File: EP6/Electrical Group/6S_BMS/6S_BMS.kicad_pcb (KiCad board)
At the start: 4 copper layers, 197 parts, among them IC1 DZDH0401DW-7, IC2 DZDH0401DW-7, J1 BATcellMain, J10 CAN1, J11 frontBox, J12 switch, J13 RESET, J14 battery cells, J2 BAT charge, J3 GLVMS, J4 24Vout, J5 USB_C_stm32, J6 UART2, J7 I2C1, J8 7seg, J9 SWD, Q1 SI2301CDS-T1-GE3, Q10 HSBA3119, Q11 2N7002, Q12 2N7002, Q13 AO3401A, Q14 2N7002, Q15 HSBA3119, Q16 HSBA3119, Q17 HSBA3119, Q2 SI2301CDS-T1-GE3, Q3 SI2301CDS-T1-GE3, Q4 SI2301CDS-T1-GE3, Q5 SI2301CDS-T1-GE3, Q6 SI2301CDS-T1-GE3, Q9 2N7002, SW1 RESET, U1 LM66100DCK, U2 BQ7693003, U3 STM32F103C8Tx, U4 78L05G-AB3-R, U5 HT7533, U6 TCAN1042VDRQ1, Y1 8MHz X49SM8MSD2SC

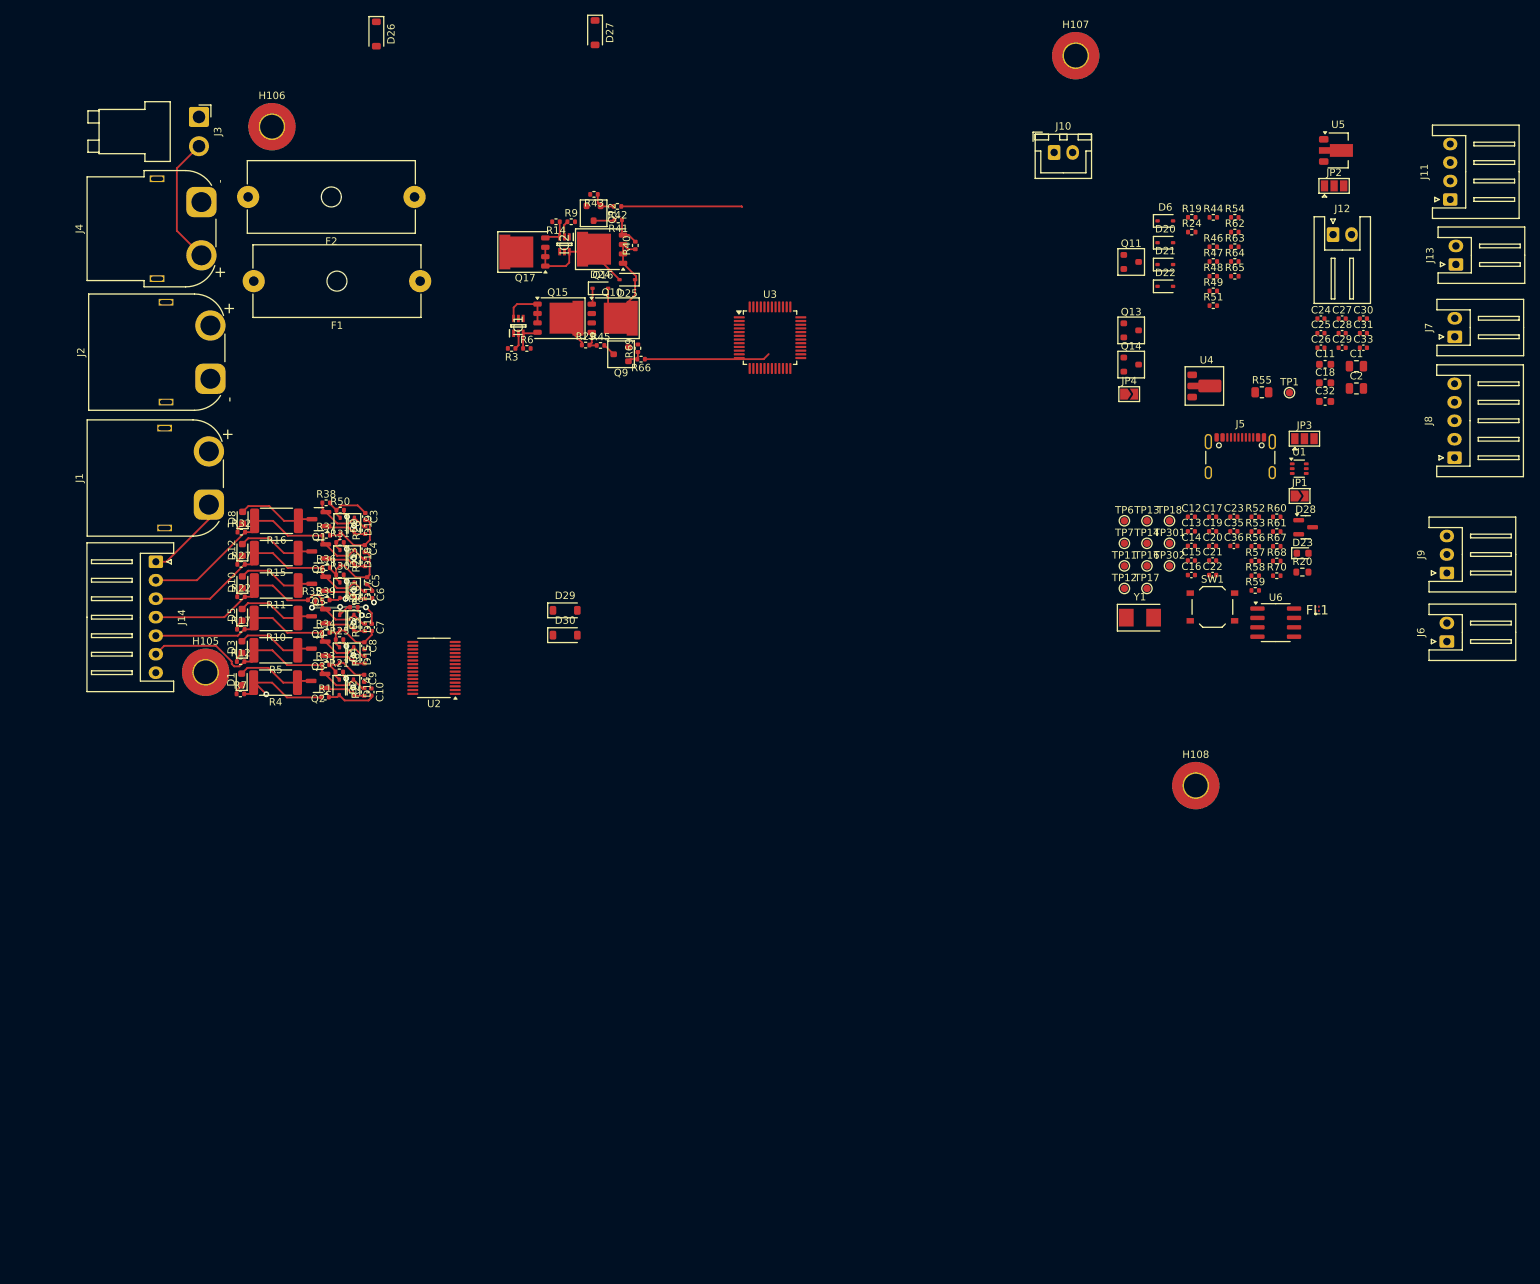
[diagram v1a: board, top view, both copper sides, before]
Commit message: added nickel tabs footprint, assigned footprints
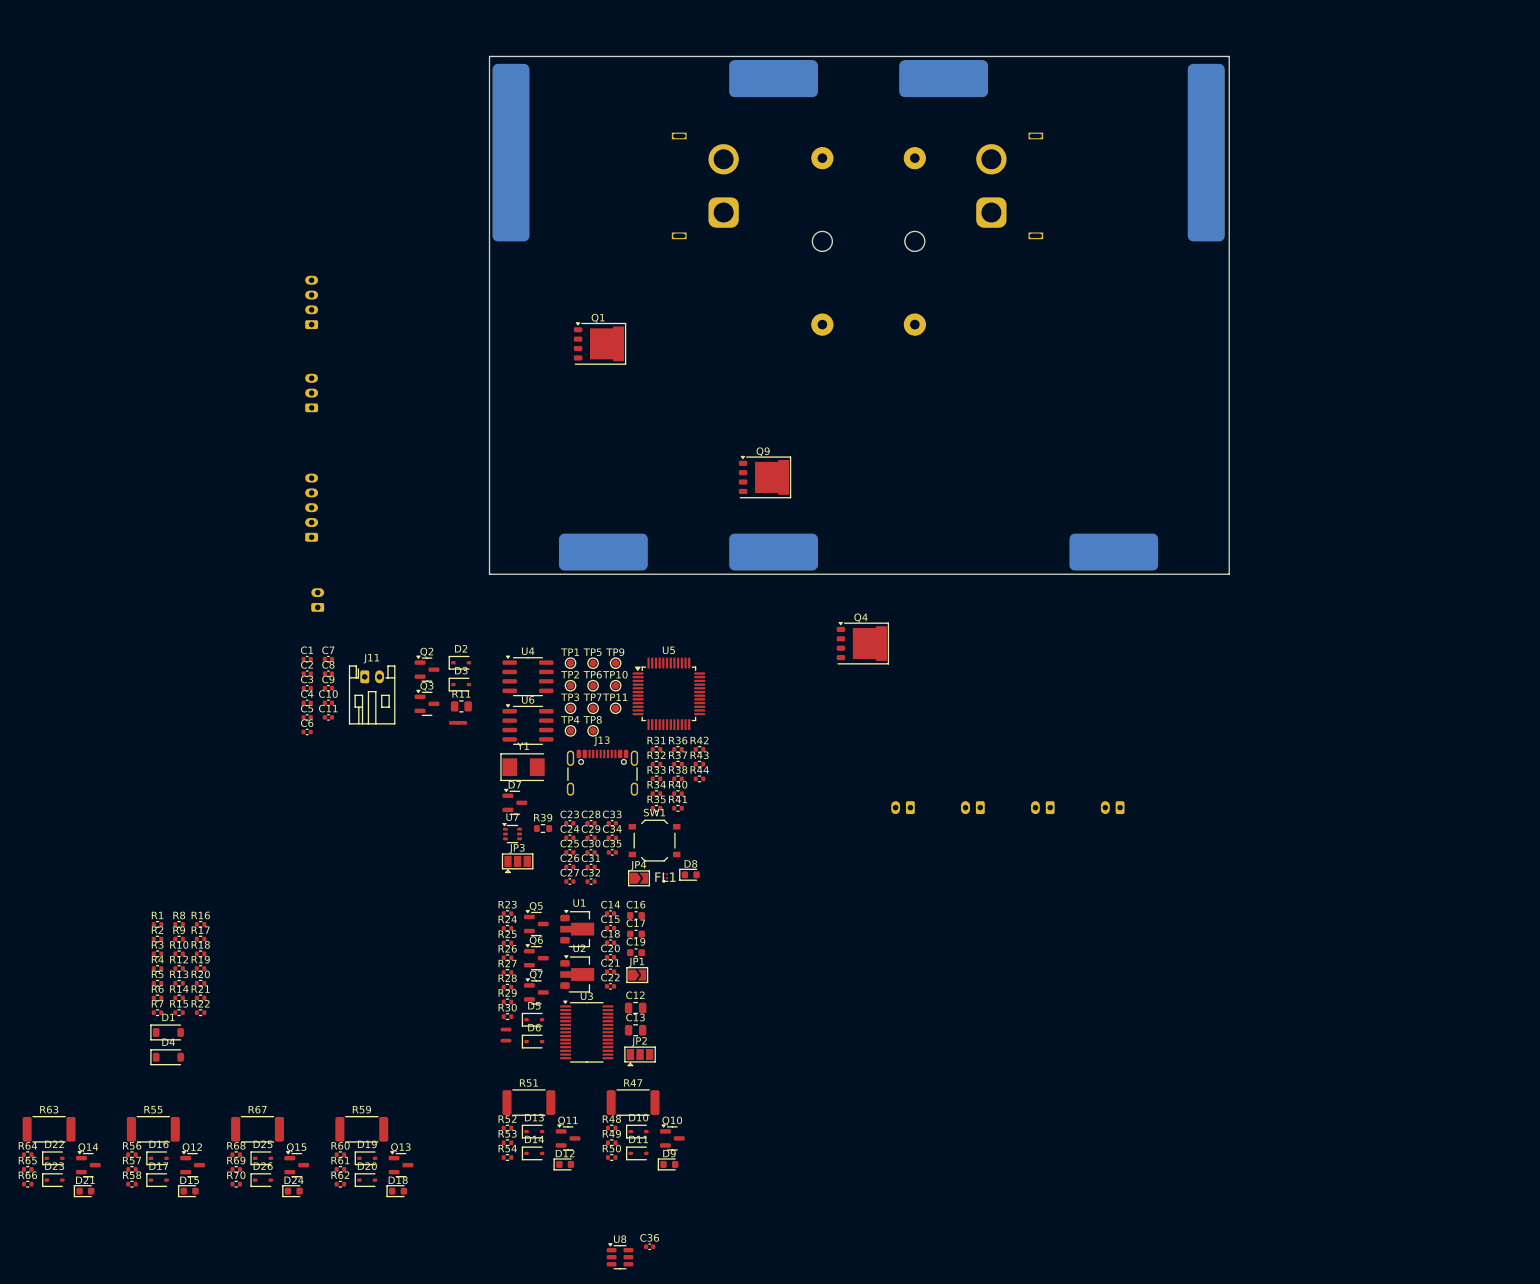
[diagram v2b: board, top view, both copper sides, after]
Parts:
- removed D27, D29, D30: 27V, Diode_SMD:D_SOD-123
- removed D28: NUP2105L, Package_TO_SOT_SMD:SOT-23
- removed H105, H106, H107, H108: MountingHole_Pad, MountingHole:MountingHole_3.2mm_M3_Pad_TopBottom
- removed IC1, IC2: DZDH0401DW-7, SamacSys_Parts_EP6:SOT65P210X110-6N
- removed J14: battery cells, Connector_JST:JST_XH_S7B-XH-A_1x07_P2.50mm_Horizontal
- removed Q16, Q17: HSBA3119, nturt_kicad_lib_EP6:HSBA3119_PRPAK5X6
- removed R45: 100k, Resistor_SMD:R_0402_1005Metric
- removed R46: 10k, Resistor_SMD:R_0402_1005Metric
- removed TP12: SPI2_MISO, TestPoint:TestPoint_Pad_D1.0mm
- removed TP13: SPI2_SCK, TestPoint:TestPoint_Pad_D1.0mm
- removed TP14: CAN1_S, TestPoint:TestPoint_Pad_D1.0mm
- removed TP16: SPI2_CSN, TestPoint:TestPoint_Pad_D1.0mm
- removed TP17: I2C1_SCL, TestPoint:TestPoint_Pad_D1.0mm
- removed TP18: I2C1_SDA, TestPoint:TestPoint_Pad_D1.0mm
- removed TP301: CAN1_RX, TestPoint:TestPoint_Pad_D1.0mm
- removed TP302: CAN1_TX, TestPoint:TestPoint_Pad_D1.0mm
- added C34: 0u1, Capacitor_SMD:C_0402_1005Metric, F.Cu at (116.6, 130.6)
- added NT1: CELL_NEG_TIE, NetTie:NetTie-3_SMD_Pad0.5mm, F.Cu at (95.7, 115.1)
- added NT2: NetTie_2, NetTie:NetTie-2_SMD_Pad0.5mm, F.Cu at (102.2, 156.6)
- added NT3: NetTie_2, NetTie:NetTie-2_SMD_Pad0.5mm, F.Cu at (102.2, 158.1)
- added Q7: AO3401A, Package_TO_SOT_SMD:SOT-23, F.Cu at (106.3, 151.5)
- added TP10: UART1_TX, TestPoint:TestPoint_Pad_D1.0mm, F.Cu at (117.1, 110.1)
- added TP2: CAN1_S, TestPoint:TestPoint_Pad_D1.0mm, F.Cu at (111.0, 110.1)
- added TP3: SPI2_CSN, TestPoint:TestPoint_Pad_D1.0mm, F.Cu at (111.0, 113.1)
- added TP4: SPI2_MISO, TestPoint:TestPoint_Pad_D1.0mm, F.Cu at (111.0, 116.2)
- added TP5: I2C1_SDA, TestPoint:TestPoint_Pad_D1.0mm, F.Cu at (114.0, 107.0)
- added TP8: SPI2_MOSI, TestPoint:TestPoint_Pad_D1.0mm, F.Cu at (114.0, 116.2)
- added TP9: CAN1_RX, TestPoint:TestPoint_Pad_D1.0mm, F.Cu at (117.1, 107.0)
- added U7: LM66100DCK, Package_TO_SOT_SMD:SOT-363_SC-70-6, F.Cu at (103.1, 130.1)
- added U8: LM74700, Package_TO_SOT_SMD:SOT-23-6, F.Cu at (117.6, 187.3)
- C1, C2: value 10u 25V -> 1u; footprint Capacitor_SMD:C_0805_2012Metric -> Capacitor_SMD:C_0402_1005Metric
- C10, C25, C26, C9: value 1u -> 0u1
- C11: value 1u -> 0u1; footprint Capacitor_SMD:C_0603_1608Metric -> Capacitor_SMD:C_0402_1005Metric
- C12, C13: value 30p -> 10u 25V; footprint Capacitor_SMD:C_0402_1005Metric -> Capacitor_SMD:C_0805_2012Metric
- C14: value 10u 6V -> 1u
- C15, C20, C21: value 0u1 -> 1u
- C16: value 10u 6V -> 10u; footprint Capacitor_SMD:C_0402_1005Metric -> Capacitor_SMD:C_0603_1608Metric
- C17: value 10u 6V -> 4u7 16V; footprint Capacitor_SMD:C_0402_1005Metric -> Capacitor_SMD:C_0603_1608Metric
- C18: value 4u7 16V -> 10u; footprint Capacitor_SMD:C_0603_1608Metric -> Capacitor_SMD:C_0402_1005Metric
- C19: value 10u 6V -> 1u; footprint Capacitor_SMD:C_0402_1005Metric -> Capacitor_SMD:C_0603_1608Metric
- C22: value 0u1 -> 470p
- C24: value 470p -> 30p
- C27: value 0u1 -> 30p
- C28, C29, C31: value 0u1 -> 10u 6V
- C30: value 1u -> 10u 6V
- C32: value 10u -> 0u1; footprint Capacitor_SMD:C_0603_1608Metric -> Capacitor_SMD:C_0402_1005Metric
- C33: value 10u -> 0u1
- C36: value 0u1 -> 220nF 25V
- D1: value RED -> 27V; footprint LED_SMD:LED_0603_1608Metric -> Diode_SMD:D_SOD-123
- D10: value RED -> BZT52C6V8S; footprint LED_SMD:LED_0603_1608Metric -> Diode_SMD:D_SOD-323
- D12: value RED -> BAL_1
- D15, D18, D9: value BZT52C6V8S -> BAL_1; footprint Diode_SMD:D_SOD-323 -> LED_SMD:LED_0603_1608Metric
- D2: value BZT52C6V8S -> 1N4148WS
- D20: value 1N4148WS -> BZT52C6V8S
- D21: value 1N4148WS -> BAL_1; footprint Diode_SMD:D_SOD-323 -> LED_SMD:LED_0603_1608Metric
- D22: value BZX584C3V3 -> BZT52C6V8S
- D23: value WHITE -> BZT52C6V8S; footprint LED_SMD:LED_0603_1608Metric -> Diode_SMD:D_SOD-323
- D24: value 27V -> BAL_1; footprint Diode_SMD:D_SOD-323 -> LED_SMD:LED_0603_1608Metric
- D25: value 27V -> BZT52C6V8S
- D26: value 27V -> BZT52C6V8S; footprint Diode_SMD:D_SOD-123 -> Diode_SMD:D_SOD-323
- D3: value RED -> BZX584C3V3; footprint LED_SMD:LED_0603_1608Metric -> Diode_SMD:D_SOD-323
- D4: value BZT52C6V8S -> 27V; footprint Diode_SMD:D_SOD-323 -> Diode_SMD:D_SOD-123
- D5: value RED -> 1N4148WS; footprint LED_SMD:LED_0603_1608Metric -> Diode_SMD:D_SOD-323
- D7: value BZT52C6V8S -> NUP2105L; footprint Diode_SMD:D_SOD-323 -> Package_TO_SOT_SMD:SOT-23
- D8: value RED -> WHITE
- F1: value 10A charge fuse -> 10A battery fuse; moved to B.Cu
- F2: value 10A discharge fuse -> 10A ext fuse; moved to B.Cu
- J1: value BATcellMain -> battery cells; footprint Connector_AMASS:AMASS_XT60PW-M_1x02_P7.20mm_Horizontal -> nturt_kicad_lib_EP6:6S_batteries_100mm_across; moved to B.Cu
- J10: value CAN1 -> I2C1; footprint Connector_JST:JST_XH_B2B-XH-A_1x02_P2.50mm_Vertical -> Connector_JST:JST_PH_S2B-PH-K_1x02_P2.00mm_Horizontal; moved to B.Cu
- J11: value frontBox -> CAN1; footprint Connector_JST:JST_XH_S4B-XH-A_1x04_P2.50mm_Horizontal -> Connector_JST:JST_PH_S2B-PH-K_1x02_P2.00mm_Horizontal
- J12: value switch -> frontBox; footprint Connector_JST:JST_XH_S2B-XH-A_1x02_P2.50mm_Horizontal -> Connector_JST:JST_PH_S4B-PH-K_1x04_P2.00mm_Horizontal; moved to B.Cu
- J13: value RESET -> USB_C_stm32; footprint Connector_JST:JST_XH_S2B-XH-A_1x02_P2.50mm_Horizontal -> Connector_USB:USB_C_Receptacle_GCT_USB4105-xx-A_16P_TopMnt_Horizontal
- J2: value BAT charge -> GLVMS; footprint Connector_AMASS:AMASS_XT60PW-M_1x02_P7.20mm_Horizontal -> Connector_JST:JST_PH_S2B-PH-K_1x02_P2.00mm_Horizontal; moved to B.Cu
- J3: value GLVMS -> BOOT_BTN; footprint Connector_JST:JST_VH_B2PS-VH_1x02_P3.96mm_Horizontal -> Connector_JST:JST_PH_S2B-PH-K_1x02_P2.00mm_Horizontal; moved to B.Cu
- J4: moved to B.Cu
- J5: value USB_C_stm32 -> CHARGE; footprint Connector_USB:USB_C_Receptacle_GCT_USB4105-xx-A_16P_TopMnt_Horizontal -> Connector_AMASS:AMASS_XT60PW-M_1x02_P7.20mm_Horizontal; moved to B.Cu
- J6: footprint Connector_JST:JST_XH_S2B-XH-A_1x02_P2.50mm_Horizontal -> Connector_JST:JST_PH_S2B-PH-K_1x02_P2.00mm_Horizontal; moved to B.Cu
- J7: value I2C1 -> SWD; footprint Connector_JST:JST_XH_S2B-XH-A_1x02_P2.50mm_Horizontal -> Connector_JST:JST_PH_S3B-PH-K_1x03_P2.00mm_Horizontal; moved to B.Cu
- J8: footprint Connector_JST:JST_XH_S5B-XH-A_1x05_P2.50mm_Horizontal -> Connector_JST:JST_PH_S5B-PH-K_1x05_P2.00mm_Horizontal; moved to B.Cu
- J9: value SWD -> RESET; footprint Connector_JST:JST_XH_S3B-XH-A_1x03_P2.50mm_Horizontal -> Connector_JST:JST_PH_S2B-PH-K_1x02_P2.00mm_Horizontal; moved to B.Cu
- JP1: value Vbus -> REGSRC bypass
- JP2: value 3V3 source -> 3V3 select
- JP4: value REGSRC bypass -> Vbus
- Q1, Q4: value SI2301CDS-T1-GE3 -> HSBA3119; footprint Package_TO_SOT_SMD:SOT-23 -> nturt_kicad_lib_EP6:HSBA3119_PRPAK5X6
- Q10, Q15: value HSBA3119 -> SI2301CDS-T1-GE3; footprint nturt_kicad_lib_EP6:HSBA3119_PRPAK5X6 -> Package_TO_SOT_SMD:SOT-23
- Q11, Q12, Q14: value 2N7002 -> SI2301CDS-T1-GE3; footprint PCM_Package_TO_SOT_SMD_AKL:SOT-23 -> Package_TO_SOT_SMD:SOT-23
- Q13: value AO3401A -> SI2301CDS-T1-GE3; footprint PCM_Package_TO_SOT_SMD_AKL:SOT-23 -> Package_TO_SOT_SMD:SOT-23
- Q2, Q3, Q5, Q6: value SI2301CDS-T1-GE3 -> 2N7002
- Q9: value 2N7002 -> HSBA3119; footprint PCM_Package_TO_SOT_SMD_AKL:SOT-23 -> nturt_kicad_lib_EP6:HSBA3119_PRPAK5X6
- R10: value 10R 2W 2512 -> 100k; footprint Resistor_SMD:R_2512_6332Metric -> Resistor_SMD:R_0402_1005Metric
- R11: value 10R 2W 2512 -> 10R 1%; footprint Resistor_SMD:R_2512_6332Metric -> Resistor_SMD:R_0805_2012Metric
- R13, R2, R8: value 2M -> 1k
- R14: value Rbias -> 100R
- R15, R16: value 10R 2W 2512 -> 1M; footprint Resistor_SMD:R_2512_6332Metric -> Resistor_SMD:R_0402_1005Metric
- R17: value 1k -> 100k
- R18: value 2M -> 100k
- R19: value 100R -> 100k
- R20: value 1k -> 4k3; footprint Resistor_SMD:R_0603_1608Metric -> Resistor_SMD:R_0402_1005Metric
- R21: value 1k -> 15k
- R22: value 1k -> 47k
- R23: value 2M -> 100R
- R26: value 1k -> 1M
- R27: value 1k -> 470k
- R28: value 2M -> 1M
- R29, R40: value 100k -> 10k
- R3: value Rref -> 1k
- R30: value 1k -> 500k
- R31, R32, R36: value 1k -> 10k
- R34, R35: value 1k -> 100R
- R37, R38: value 1k -> 4k7
- R39: footprint Resistor_SMD:R_0402_1005Metric -> Resistor_SMD:R_0603_1608Metric
- R4, R5: value 10R 2W 2512 -> 1k; footprint Resistor_SMD:R_2512_6332Metric -> Resistor_SMD:R_0402_1005Metric
- R41: value 100k -> 10R
- R42: value 1k -> 10R
- R43: value 1M -> 5k1
- R44: value 500k -> 5k1
- R47: value 10k -> 10R 2W 2512; footprint Resistor_SMD:R_0402_1005Metric -> Resistor_SMD:R_2512_6332Metric
- R48, R52, R56, R70: value 10k -> 1k
- R49, R53: value 10k -> 2M
- R51, R67: value 100R -> 10R 2W 2512; footprint Resistor_SMD:R_0402_1005Metric -> Resistor_SMD:R_2512_6332Metric
- R54, R68: value 100R -> 1k
- R55: value 10R 1% -> 10R 2W 2512; footprint Resistor_SMD:R_0805_2012Metric -> Resistor_SMD:R_2512_6332Metric
- R57: value 5k1 -> 2M
- R58: value 5k1 -> 1k
- R59: value 10R -> 10R 2W 2512; footprint Resistor_SMD:R_0402_1005Metric -> Resistor_SMD:R_2512_6332Metric
- R6: value Rbias -> 1k
- R60: value 10R -> 1k
- R61: value 1k -> 2M
- R62: value 1M -> 1k
- R63: value 1M -> 10R 2W 2512; footprint Resistor_SMD:R_0402_1005Metric -> Resistor_SMD:R_2512_6332Metric
- R65, R69: value 1M -> 2M
- R9: value Rref -> 100R
- TP1: value REGOUT -> I2C1_SCL
- TP11: value SPI2_MOSI -> UART1_RX
- TP6: value UART1_TX -> CAN1_TX
- TP7: value UART1_RX -> SPI2_SCK
- U1: value LM66100DCK -> 78L05G-AB3-R; footprint Package_TO_SOT_SMD:SOT-363_SC-70-6 -> Package_TO_SOT_SMD:SOT-89-3
- U2: value BQ7693003 -> HT7533; footprint Package_SO:TSSOP-30_4.4x7.8mm_P0.5mm -> Package_TO_SOT_SMD:SOT-89-3
- U3: value STM32F103C8Tx -> BQ7693003; footprint Package_QFP:LQFP-48_7x7mm_P0.5mm -> Package_SO:TSSOP-30_4.4x7.8mm_P0.5mm
- U4: value 78L05G-AB3-R -> TCAN1042VDRQ1; footprint PCM_Package_TO_SOT_SMD_AKL:SOT-89-3 -> Package_SO:SOIC-8_3.9x4.9mm_P1.27mm
- U5: value HT7533 -> STM32F103C8Tx; footprint Package_TO_SOT_SMD:SOT-89-3 -> Package_QFP:LQFP-48_7x7mm_P0.5mm
- U6: value TCAN1042VDRQ1 -> CAT24C256
- moved R64 203.0 mm to (37.6, 173.5)
- moved R65 203.0 mm to (37.6, 175.5)
- moved R63 199.8 mm to (40.5, 170.0)
- moved D21 192.4 mm to (45.4, 178.4)
- moved D22 190.9 mm to (41.2, 174.0)
- moved D23 188.8 mm to (41.2, 176.9)
- moved R55 180.0 mm to (54.6, 170.0)
- moved Q14 177.7 mm to (45.8, 174.9)
- moved R62 176.6 mm to (79.8, 177.5)
- moved R56 172.7 mm to (51.7, 173.5)
- moved R58 172.7 mm to (51.7, 177.5)
- moved R57 172.7 mm to (51.7, 175.5)
- moved R19 168.1 mm to (60.9, 148.3)
- moved D20 166.4 mm to (83.5, 176.9)
- moved R70 163.0 mm to (65.8, 177.5)
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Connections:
- C1 pad 1: /AFE/VC5X -> /C6
- C1 pad 2: /AFE/BAT -> /C5
- C10 pad 1: GND -> /SRP
- C10 pad 2: /AFE/C0 -> /SRN
- C11 pad 2: /AFE/REGSRC -> /SRN
- C12 pad 1: /MCU/OSC_IN -> /VC5X
- C12 pad 2: GND -> /AFE/BAT
- C13 pad 1: /MCU/OSC_OUT -> GND
- C13 pad 2: GND -> /VC5X
- C14 pad 1: +3V3 -> GND
- C14 pad 2: GND -> Net-(Q7-D)
- C15 pad 1: /MCU/NRST -> GND
- C15 pad 2: GND -> +5V
- C16 pad 1: +3V3 -> GND
- C16 pad 2: GND -> +5V
- C17 pad 1: +3V3 -> GND
- C17 pad 2: GND -> /AFE/REGOUT
- C18 pad 2: /AFE/REGOUT -> /AFE/LDO_3V3
- C19 pad 1: +3V3 -> /AFE/REGSRC
- C2 pad 1: GND -> /C5
- C2 pad 2: /AFE/VC5X -> /C4
- C20 pad 1: +3V3 -> /VC5X
- C20 pad 2: GND -> Net-(U3-CAP2)
- C21 pad 1: +3V3 -> Net-(U3-CAP1)
- C22 pad 1: +3V3 -> /ALERT
- C23 pad 1: +3V3 -> +5V
- C24 pad 1: Net-(U2-ALERT) -> /MCU/OSC_IN
- C25 pad 1: /AFE/VC5X -> +3V3
- C25 pad 2: Net-(U2-CAP2) -> GND
- C26 pad 1: Net-(U2-CAP1) -> /MCU/NRST
- C27 pad 1: /AFE/SRP -> /MCU/OSC_OUT
- C27 pad 2: /AFE/SRN -> GND
- C28 pad 1: GND -> +3V3
- C28 pad 2: /AFE/SRP -> GND
- C29 pad 1: GND -> +3V3
- C29 pad 2: /AFE/SRN -> GND
- C3 pad 1: /AFE/C6 -> /C4
- C3 pad 2: /AFE/C5 -> /VC5X
- C30 pad 1: GND -> +3V3
- C30 pad 2: Net-(Q13-D) -> GND
- C31 pad 1: GND -> +3V3
- C31 pad 2: +5V -> GND
- C32 pad 1: GND -> +3V3
- C32 pad 2: +5V -> GND
- C33 pad 1: GND -> +3V3
- C33 pad 2: Net-(JP2-A) -> GND
- C35 pad 1: +5V -> +3V3
- C36 pad 1: +3V3 -> /EXT Ideal Diode/A
- C36 pad 2: GND -> Net-(U8-VCAP)
- C4 pad 1: /AFE/C5 -> /VC5X
- C4 pad 2: /AFE/C4 -> /C3.5
- C5 pad 1: /AFE/C4 -> /C3
- C5 pad 2: /AFE/VC5X -> /C2
- C6 pad 1: /AFE/VC5X -> /C2
- C6 pad 2: /AFE/VC5B -> /C1
- C7 pad 1: /AFE/C3 -> /C1
- C7 pad 2: /AFE/C2 -> GND
- C8 pad 1: /AFE/C2 -> GND
- C8 pad 2: /AFE/C1 -> /C0
- C9 pad 1: /AFE/C1 -> GND
- C9 pad 2: GND -> /SRP
- D1 pad 1: Net-(D1-K) -> /PACK+
- D1 pad 2: Net-(D1-A) -> GND
- D10 pad 1: Net-(D10-K) -> /CT6
- D11 pad 1: /AFE/C4 -> /C6
- D11 pad 2: /AFE/VC5B -> /C5
- D13 pad 1: /AFE/C5 -> /CT5
- D13 pad 2: /AFE/C4 -> Net-(D13-A)
- D14 pad 1: /balancing/CT1 -> /C5
- D14 pad 2: Net-(D14-A) -> /C4
- D15 pad 1: /balancing/CT2 -> Net-(D15-K)
- D16 pad 1: /balancing/CT3 -> /CT4
- D17 pad 1: /balancing/CT4 -> /C4
- D17 pad 2: Net-(D17-A) -> /C3.5
- D18 pad 1: /balancing/CT5 -> Net-(D18-K)
- D19 pad 1: /balancing/CT6 -> /CT3
- D2 pad 1: /AFE/C1 -> Net-(D2-K)
- D2 pad 2: /AFE/C0 -> Net-(D2-A)
- D20 pad 1: /AFE/BAT -> /C3
- D20 pad 2: /AFE/C6 -> /C2
- D22 pad 1: Net-(D22-K) -> /CT2
- D22 pad 2: GND -> Net-(D22-A)
- D23 pad 1: Net-(D23-K) -> /C2
- D23 pad 2: /MCU/led -> /C1
- D24 pad 1: /AFE/D_ideal/Vout -> Net-(D24-K)
- D24 pad 2: /balancing/CT6 -> Net-(D24-A)
- D25 pad 1: /balancing/CT6 -> /CT1
- D25 pad 2: /AFE/D_ideal1/Vin -> Net-(D25-A)
- D26 pad 1: /AFE/D_ideal/Vin -> /C1
- D26 pad 2: GND -> /C0
- D3 pad 2: Net-(D3-A) -> GND
- D4 pad 1: /AFE/C2 -> /EXT Ideal Diode/A
- D4 pad 2: /AFE/C1 -> GND
- D5 pad 1: Net-(D5-K) -> /VC5X
- D5 pad 2: Net-(D5-A) -> /AFE/VC5
- D6 pad 1: /AFE/VC5X -> /AFE/BAT
- D6 pad 2: /AFE/C3 -> /AFE/VC10
- D7 pad 1: /AFE/C3 -> /CANL
- D7 pad 2: /AFE/C2 -> /CANH
- D8 pad 2: Net-(D8-A) -> /MCU/led
- D9 pad 1: /AFE/C6 -> Net-(D9-K)
- D9 pad 2: /AFE/C5 -> Net-(D9-A)
- F1 pad 1: /AFE/D_ideal/Vin -> /CT6
- F1 pad 2: /CHARGE -> /CELLS+
- F2 pad 1: /AFE/D_ideal1/Vout -> /CHG_EXT
- F2 pad 2: /AFE/DISCHARGE -> /EXT Ideal Diode/A
- FL1 pad 1: Net-(U6-CANH) -> Net-(U4-CANH)
- FL1 pad 2: Net-(U6-CANL) -> Net-(U4-CANL)
- J1 pad 1: /balancing/CT6 -> /CT0
- J1 pad 2: GND -> /CT1
- J10 pad 1: /CANH -> /SCL
- J10 pad 2: /CANL -> /SDA
- J12 pad 1: Net-(D21-A) -> /CANH
- J12 pad 2: /balancing/CT6 -> /CANL
- J2 pad 1: /PACK- -> /PACK+
- J2 pad 2: /CHARGE -> +24V
- J3 pad 1: /AFE/DISCHARGE -> /CELLS+
- J3 pad 2: +24V -> Net-(D2-A)
- J7 pad 1: /SCL -> GND
- J7 pad 2: /SDA -> /MCU/SWCLK
- J8 pad 2: /MCU/SPI2_SCK -> /MCU/SPI2_MOSI
- J8 pad 4: /MCU/SPI2_MOSI -> /MCU/SPI2_SCK
- J9 pad 2: /MCU/SWCLK -> /MCU/NRST
- JP1 pad 1: Net-(JP1-A) -> /AFE/REGSRC
- JP1 pad 2: +5V -> /CELLS+
- JP2 pad 1: Net-(JP2-A) -> /AFE/LDO_3V3
- JP3 pad 2: unconnected-(R61-Pad1) -> Net-(JP3-C)
- JP4 pad 1: /AFE/REGSRC -> Net-(JP4-A)
- JP4 pad 2: /balancing/CT6 -> +5V
- Q11 pad 1: /AFE/VC5X -> Net-(D13-A)
- Q11 pad 2: /AFE/REGSRC -> /CT5
- Q11 pad 3: /balancing/CT6 -> Net-(D12-A)
- Q12 pad 1: Net-(Q12-G) -> Net-(D16-A)
- Q12 pad 2: GND -> /CT4
- Q12 pad 3: Net-(Q12-D) -> Net-(D15-A)
- Q13 pad 1: Net-(Q13-G) -> Net-(D19-A)
- Q13 pad 2: /balancing/CT6 -> /CT3
- Q13 pad 3: Net-(Q13-D) -> Net-(D18-A)
- Q14 pad 1: Net-(Q14-G) -> Net-(D22-A)
- Q14 pad 2: GND -> /CT2
- Q14 pad 3: Net-(Q14-D) -> Net-(D21-A)
- Q2 pad 1: Net-(D14-A) -> Net-(Q2-G)
- Q2 pad 2: /balancing/CT1 -> GND
- Q2 pad 3: Net-(D1-A) -> Net-(Q2-D)
- Q3 pad 1: Net-(D15-A) -> Net-(Q3-G)
- Q3 pad 2: /balancing/CT2 -> GND
- Q3 pad 3: Net-(D3-A) -> Net-(Q3-D)
- Q5 pad 1: Net-(D17-A) -> /VC5X
- Q5 pad 2: /balancing/CT4 -> /AFE/REGSRC
- Q5 pad 3: Net-(D10-A) -> /CELLS+
- Q6 pad 1: Net-(D18-A) -> Net-(Q6-G)
- Q6 pad 2: /balancing/CT5 -> GND
- Q6 pad 3: Net-(D12-A) -> Net-(Q6-D)
- R1 pad 1: GND -> /CT6
- R1 pad 2: /AFE/C0 -> /C6
- R10 pad 1: Net-(D5-A) -> Net-(Q1-PadS)
- R10 pad 2: /balancing/CT2 -> /CHG_G
- R11 pad 1: Net-(D10-A) -> /CELLS-
- R11 pad 2: /balancing/CT3 -> /PACK-
- R12 pad 1: Net-(D3-K) -> /CHG_EN
- R12 pad 2: /balancing/CT1 -> Net-(Q2-G)
- R13 pad 1: Net-(D16-A) -> /DSC_EN
- R13 pad 2: /balancing/CT3 -> Net-(Q3-G)
- R14 pad 1: Net-(IC2-BIAS) -> /PACK-
- R14 pad 2: GND -> /SRN
- R15 pad 1: Net-(D12-A) -> Net-(Q2-G)
- R15 pad 2: /balancing/CT4 -> GND
- R16 pad 1: Net-(D8-A) -> Net-(Q3-G)
- R16 pad 2: /balancing/CT5 -> GND
- R17 pad 1: Net-(D5-K) -> Net-(Q1-PadS)
- R17 pad 2: /balancing/CT2 -> /DSC_G
- R18 pad 1: Net-(D17-A) -> /CHG_G
- R18 pad 2: /balancing/CT4 -> Net-(Q2-D)
- R19 pad 1: /AFE/VC5X -> /DSC_G
- R19 pad 2: /balancing/CT3 -> Net-(Q3-D)
- R2 pad 1: Net-(D14-A) -> /CT5
- R2 pad 2: /balancing/CT1 -> /C5
- R20 pad 1: Net-(D23-K) -> Net-(D2-K)
- R20 pad 2: GND -> Net-(D3-K)
- R21 pad 1: /AFE/C1 -> /BOOT_BTN
- R21 pad 2: Net-(D14-A) -> Net-(D3-K)
- R22 pad 1: Net-(D10-K) -> /BOOT_BTN
- R22 pad 2: /balancing/CT3 -> GND
- R23 pad 1: Net-(D18-A) -> /AFE/BAT
- R23 pad 2: /balancing/CT5 -> /CELLS+
- R24 pad 1: /AFE/BAT -> /CT3
- R24 pad 2: /balancing/CT6 -> /VC5X
- R25 pad 1: /AFE/C2 -> /AFE/REGOUT
- R25 pad 2: Net-(D15-A) -> Net-(Q6-G)
- R26 pad 1: /AFE/C3 -> Net-(Q6-G)
- R26 pad 2: Net-(D16-A) -> GND
- R27 pad 1: Net-(D12-K) -> /CELLS+
- R27 pad 2: /balancing/CT4 -> Net-(Q7-G)
- R28 pad 1: Net-(D19-A) -> Net-(Q7-G)
- R28 pad 2: /balancing/CT6 -> Net-(Q6-D)
- R29 pad 1: /AFE/D_ideal/Vout -> Net-(U3-TS2)
- R29 pad 2: Net-(Q10-PadG) -> /VC5X
- R3 pad 1: Net-(IC1-REF) -> /CT4
- R3 pad 2: GND -> /C4
- R30 pad 1: /AFE/C4 -> GND
- R30 pad 2: Net-(D17-A) -> /ALERT
- R31 pad 1: /AFE/C5 -> +3V3
- R31 pad 2: Net-(D18-A) -> /SDA
- R32 pad 1: Net-(D8-K) -> +3V3
- R32 pad 2: /balancing/CT5 -> /SCL
- R33 pad 1: /balancing/CT1 -> Net-(JP3-C)
- R33 pad 2: /AFE/C1 -> /MCU/BOOT0
- R34 pad 1: /balancing/CT2 -> /MCU/CAN1_TX
- R34 pad 2: /AFE/C2 -> Net-(U4-TXD)
- R35 pad 1: /balancing/CT3 -> /MCU/CAN1_RX
- R35 pad 2: /AFE/C3 -> Net-(U4-RXD)
- R36 pad 1: /balancing/CT4 -> Net-(U4-STB)
- R36 pad 2: /AFE/C4 -> GND
- R37 pad 1: /balancing/CT5 -> +3V3
- R37 pad 2: /AFE/C5 -> /SCL
- R38 pad 1: /balancing/CT6 -> +3V3
- R38 pad 2: /AFE/C6 -> /SDA
- R39 pad 1: /balancing/CT3 -> Net-(D8-K)
- R39 pad 2: /AFE/VC5B -> GND
- R4 pad 1: Net-(D1-A) -> /CT3
- R4 pad 2: GND -> /C3.5
- R40 pad 1: /balancing/CT6 -> Net-(JP4-A)
- R40 pad 2: Net-(Q16-PadG) -> Net-(U7-ST)
- R41 pad 1: Net-(Q16-PadG) -> /MCU/USB_DN
- R41 pad 2: Net-(Q12-D) -> /MCU/USB_D-
- R42 pad 1: /AFE/DSG_EN -> /MCU/USB_DP
- R42 pad 2: Net-(Q12-G) -> /MCU/USB_D+
- R43 pad 1: Net-(Q12-G) -> GND
- R43 pad 2: GND -> Net-(J13-CC1)
- R44 pad 1: Net-(U2-ALERT) -> GND
- R44 pad 2: /AFE/ALERT -> Net-(J13-CC2)
- R47 pad 1: /AFE/TS1 -> Net-(D9-A)
- R47 pad 2: GND -> /CT5
- R48 pad 1: /AFE/TS1 -> Net-(D9-K)
- R48 pad 2: Net-(D22-K) -> /CT5
- R49 pad 1: Net-(D22-K) -> Net-(D10-A)
- R49 pad 2: Net-(D21-K) -> /CT6
- R5 pad 1: Net-(D3-A) -> /CT3
- R5 pad 2: /balancing/CT1 -> /C3
- R50 pad 1: /AFE/C6 -> /C6
- R50 pad 2: Net-(D19-A) -> Net-(D10-A)
- R51 pad 1: /AFE/SRP -> Net-(D12-A)
- R51 pad 2: GND -> /CT4
- R52 pad 1: +3V3 -> Net-(D12-K)
- R52 pad 2: /SDA -> /CT4
- R53 pad 1: +3V3 -> Net-(D13-A)
- R53 pad 2: /SCL -> /CT5
- R54 pad 1: /AFE/SRN -> /C5
- R54 pad 2: /PACK- -> Net-(D13-A)
- R55 pad 1: GND -> Net-(D15-A)
- R55 pad 2: /PACK- -> /CT3
- R56 pad 1: Net-(JP1-A) -> Net-(D15-K)
- R56 pad 2: Net-(U1-ST) -> /CT3
- R57 pad 1: GND -> Net-(D16-A)
- R57 pad 2: Net-(J5-CC1) -> /CT4
- R58 pad 1: GND -> /C4
- R58 pad 2: Net-(J5-CC2) -> Net-(D16-A)
- R59 pad 1: /MCU/USB_DN -> Net-(D18-A)
- R59 pad 2: /MCU/USB_D- -> /CT2
- R6 pad 1: Net-(IC1-BIAS) -> /CT2
- R6 pad 2: GND -> /C2
- R60 pad 1: /MCU/USB_DP -> Net-(D18-K)
- R60 pad 2: /MCU/USB_D+ -> /CT2
- R61 pad 1: unconnected-(R61-Pad1) -> Net-(D19-A)
- R61 pad 2: /MCU/BOOT0 -> /CT3
- R62 pad 1: /balancing/CT6 -> /C3
- R62 pad 2: Net-(Q13-G) -> Net-(D19-A)
- R63 pad 1: Net-(Q13-G) -> Net-(D21-A)
- R63 pad 2: Net-(Q14-D) -> /CT1
- R64 pad 1: /AFE/REGOUT -> Net-(D21-K)
- R64 pad 2: Net-(Q14-G) -> /CT1
- R65 pad 1: Net-(Q14-G) -> Net-(D22-A)
- R65 pad 2: GND -> /CT2
- R66 pad 1: /AFE/CHG_EN -> /C2
- R66 pad 2: Net-(Q9-G) -> Net-(D22-A)
- R67 pad 1: /MCU/CAN1_TX -> Net-(D24-A)
- R67 pad 2: Net-(U6-TXD) -> /CT0
- R68 pad 1: /MCU/CAN1_RX -> Net-(D24-K)
- R68 pad 2: Net-(U6-RXD) -> /CT0
- R69 pad 1: Net-(Q9-G) -> Net-(D25-A)
- R69 pad 2: GND -> /CT1
- R7 pad 1: Net-(D1-K) -> /CT1
- R7 pad 2: GND -> /C1
- R70 pad 1: Net-(U6-STB) -> /C1
- R70 pad 2: GND -> Net-(D25-A)
- R8 pad 1: Net-(D15-A) -> /CT0
- R8 pad 2: /balancing/CT2 -> /C0
- R9 pad 1: Net-(IC2-REF) -> /CELLS-
- R9 pad 2: GND -> /SRP
- TP1 pad 1: /AFE/REGOUT -> /SCL
- TP11 pad 1: /MCU/SPI2_MOSI -> /MCU/UART1_RX
- TP6 pad 1: /MCU/UART1_TX -> /MCU/CAN1_TX
- TP7 pad 1: /MCU/UART1_RX -> /MCU/SPI2_SCK
- U1 pad 1: /MCU/VBUS -> +5V
- U1 pad 3: Net-(JP1-A) -> Net-(Q7-D)
- U2 pad 1: /AFE/DSG_EN -> GND
- U2 pad 2: /AFE/CHG_EN -> +5V
- U2 pad 3: GND -> /AFE/LDO_3V3
- U3 pad 1: +3V3 -> /DSC_EN
- U3 pad 10: (no net) -> /VC5X
- U3 pad 11: (no net) -> Net-(U3-CAP2)
- U3 pad 12: /MCU/UART2_TX -> Net-(U3-CAP2)
- U3 pad 13: /MCU/UART2_RX -> Net-(U3-TS2)
- U3 pad 14: (no net) -> Net-(U3-CAP2)
- U3 pad 15: /AFE/ALERT -> /AFE/BAT
- U3 pad 16: /AFE/TS1 -> /AFE/VC10
- U3 pad 17: /MCU/led -> /C5
- U3 pad 18: (no net) -> /C5
- U3 pad 19: (no net) -> /C5
- U3 pad 2: (no net) -> /CHG_EN
- U3 pad 20: (no net) -> /C4
- U3 pad 21: /MCU/CAN1_S -> /C3.5
- U3 pad 22: (no net) -> /AFE/VC5
- U3 pad 23: GND -> /C2
- U3 pad 24: +3V3 -> /C2
- U3 pad 25: /MCU/SPI2_CS -> /C2
- U3 pad 26: /MCU/SPI2_SCK -> /C1
- U3 pad 27: /MCU/SPI2_MISO -> /C0
- U3 pad 28: /MCU/SPI2_MOSI -> /SRP
- U3 pad 29: (no net) -> /SRN
- U3 pad 3: (no net) -> GND
- U3 pad 30: /MCU/UART1_TX -> /ALERT
- U3 pad 4: (no net) -> /SDA
- U3 pad 5: /MCU/OSC_IN -> /SCL
- U3 pad 6: /MCU/OSC_OUT -> /BOOT_BTN
- U3 pad 7: /MCU/NRST -> Net-(U3-CAP1)
- U3 pad 8: GND -> /AFE/REGOUT
- U3 pad 9: +3V3 -> /AFE/REGSRC
- U4 pad 1: +5V -> Net-(U4-TXD)
- U4 pad 3: Net-(Q13-D) -> +5V
- U5 pad 1: GND -> +3V3
- U5 pad 2: +5V -> unconnected-(U5-PC13-Pad2)
- U5 pad 3: Net-(JP2-A) -> unconnected-(U5-PC14-Pad3)
- U6 pad 1: Net-(U6-TXD) -> unconnected-(U6-A0-Pad1)
- U6 pad 2: GND -> unconnected-(U6-A1-Pad2)
- U6 pad 3: +5V -> unconnected-(U6-A2-Pad3)
- U6 pad 4: Net-(U6-RXD) -> GND
- U6 pad 5: +3V3 -> /SDA
- U6 pad 6: Net-(U6-CANL) -> /SCL
- U6 pad 7: Net-(U6-CANH) -> unconnected-(U6-WP-Pad7)
- U6 pad 8: Net-(U6-STB) -> +3V3
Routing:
- net /balancing/CT6: track 38.0 -> 0.00 mm
- net /balancing/CT5: track 35.6 -> 0.00 mm
- net /balancing/CT1: track 34.9 -> 0.00 mm
- net /balancing/CT4: track 34.8 -> 0.00 mm
- net /balancing/CT3: track 34.5 -> 0.00 mm
- net /balancing/CT2: track 33.2 -> 0.00 mm
- net +24V: track 17.4 -> 0.00 mm
- net /AFE/D_ideal1/Vin: track 17.2 -> 0.00 mm
- net /AFE/CHG_EN: track 17.0 -> 0.00 mm
- net /AFE/DSG_EN: track 16.4 -> 0.00 mm
- net GND: track 15.0 -> 0.00 mm, vias 1 -> 0
- net /AFE/C3: track 14.1 -> 0.00 mm, vias 3 -> 0
- net /AFE/C5: track 12.4 -> 0.00 mm
- net /AFE/C4: track 12.3 -> 0.00 mm
- net Net-(D8-A): track 10.6 -> 0.00 mm
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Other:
- board outline added: 100 x 70 mm
